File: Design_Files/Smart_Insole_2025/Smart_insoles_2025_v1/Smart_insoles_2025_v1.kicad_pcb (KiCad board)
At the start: 4 copper layers, 69.7 x 30.1 mm, 101 parts, among them IC1 USBLC6-2SC6, J1 Conn_01x20, J2 USB_C_Receptacle_USB2.0_16P, J4 S2B-PH-SM4-TB_LF__SN_, Q2 FDN306P, SW1 RESET, SW2 BOOT, SW3 SW_Nidec_CAS-120A1, U1 ME6211C33M5, U2 CD74HC4067M96, U3 LSM6DSO32TR, U5 ESP32-C3-MINI-1-N4, U7 BQ24040DSQR, U8 MCP6004-I_ST, U9 MCP6004-I_ST

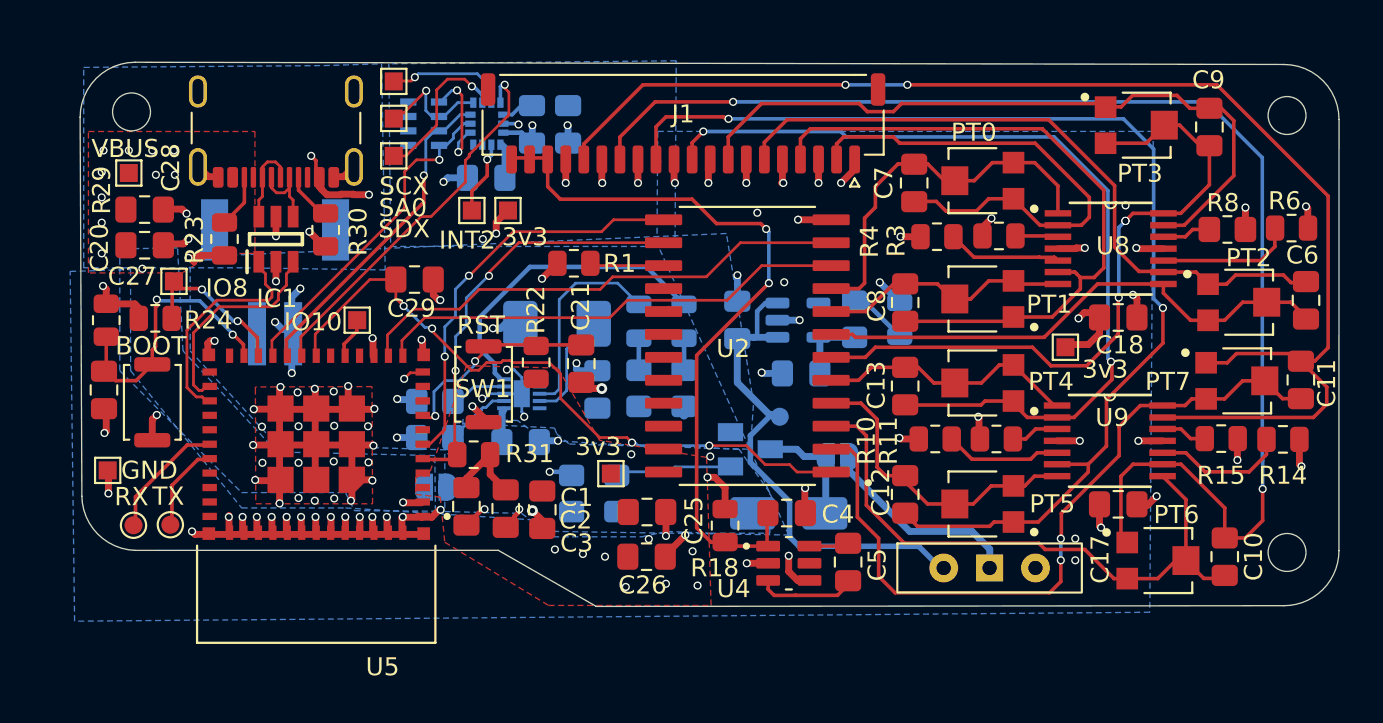
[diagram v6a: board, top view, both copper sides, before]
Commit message: PCB:Fixed Multiplexer wrong footprint. Flex Connector modified. Fixed DRC Errors and Warnings
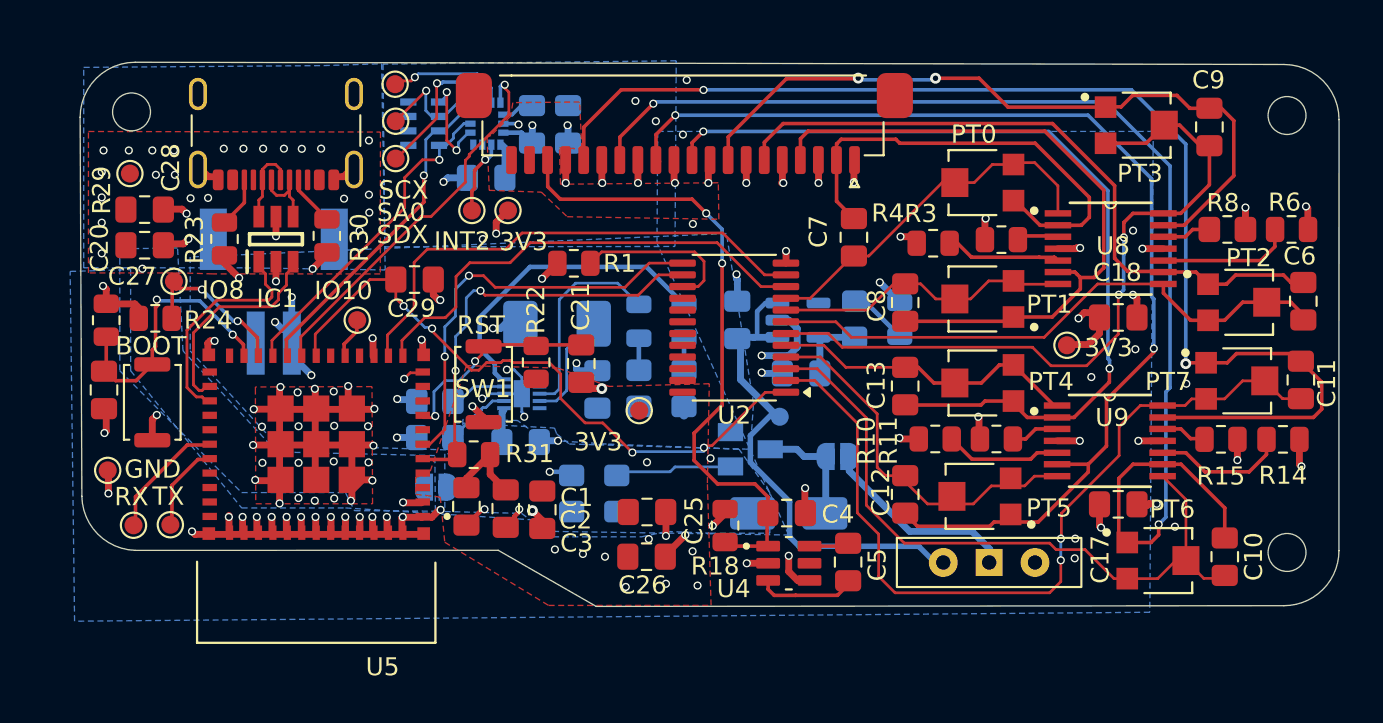
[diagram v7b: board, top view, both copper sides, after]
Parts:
- removed 3v3 (x3), GND, INT2, IO10, IO8, SA0, SCX, SDX, VBUS: TestPoint_Alt, TestPoint:TestPoint_Pad_1.0x1.0mm
- added TP1: TestPoint_Alt, TestPoint:TestPoint_Pad_D1.0mm, F.Cu at (106.3, 91.5)
- added TP10: TestPoint_Alt, TestPoint:TestPoint_Pad_D1.0mm, F.Cu at (122.2, 70.1)
- added TP11: TestPoint_Alt, TestPoint:TestPoint_Pad_D1.0mm, F.Cu at (126.5, 77.1)
- added TP12: TestPoint_Alt, TestPoint:TestPoint_Pad_D1.0mm, F.Cu at (135.8, 88.2)
- added TP13: TestPoint_Alt, TestPoint:TestPoint_Pad_D1.0mm, F.Cu at (159.5, 84.6)
- added TP14: TestPoint_Alt, TestPoint:TestPoint_Pad_D1.0mm, F.Cu at (122.3, 72.2)
- added TP2: TestPoint_Alt, TestPoint:TestPoint_Pad_D1.0mm, F.Cu at (128.5, 77.1)
- added TP3: TestPoint_Alt, TestPoint:TestPoint_Pad_D1.0mm, F.Cu at (107.6, 75.1)
- added TP7: TestPoint_Alt, TestPoint:TestPoint_Pad_D1.0mm, F.Cu at (110.0, 81.0)
- added TP8: TestPoint_Alt, TestPoint:TestPoint_Pad_D1.0mm, F.Cu at (120.2, 83.2)
- added TP9: TestPoint_Alt, TestPoint:TestPoint_Pad_D1.0mm, F.Cu at (122.3, 74.2)
- J2: footprint Connector_USB:USB_C_Receptacle_GCT_USB4105-xx-A_16P_TopMnt_Horizontal -> USB_C_Receptacle_16P_SMD_pins_THT_mech:USB_C_Receptacle_GCT_USB4105-xx-A_16P_TopMnt_Horizontal
- U2: footprint CD74HC4067:SOIC127P1030X265-24N -> Package_SO:TSSOP-24_4.4x7.8mm_P0.65mm
- moved C7 4.50 mm to (147.7, 78.6), turned to -90 degrees
- moved U2 1.24 mm to (141.0, 83.6)
- moved J4 0.52 mm to (115.5, 84.5)
- moved PT5 0.45 mm to (154.5, 93.0)
- moved R4 0.42 mm to (152.1, 78.9)
- moved R30 0.34 mm to (118.5, 78.5)
- moved SW3 0.31 mm to (155.2, 96.6)
- moved R3 0.25 mm to (155.8, 78.7)
- moved C6 0.16 mm to (172.6, 82.2)
- moved J2 0.14 mm to (115.7, 71.8)
- moved PT0 0.11 mm to (154.7, 75.6)
- moved R6 0.08 mm to (171.9, 78.2)
- renumbered VSEL to TP4
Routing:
- net /FSR_AnalogFE/FSR_OUT_7: track 74.1 -> 68.2 mm
- net Net-(U2-~{E}): track 3.96 -> 9.30 mm
- net I7: track 40.9 -> 46.1 mm
- net /FSR_AnalogFE/FSR_OUT_6: track 73.9 -> 69.1 mm
- net /FSR_AnalogFE/FSR_IN: track 41.3 -> 36.7 mm
- net VBUS: track 6.06 -> 1.49 mm, vias 14 -> 25
- net I6: track 33.7 -> 38.1 mm
- net I5: track 16.8 -> 21.1 mm
- net I2: track 29.6 -> 32.4 mm
- net I4: track 14.5 -> 17.2 mm
- net I3: track 38.0 -> 40.6 mm, vias 3 -> 2
- net I1: track 14.0 -> 16.5 mm
- net /FSR_AnalogFE/FSR_OUT_0: track 28.3 -> 26.5 mm
- net /FSR_AnalogFE/FSR_OUT_5: track 64.3 -> 62.7 mm
- net SIG: track 37.9 -> 36.4 mm
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- added copper zone on F.Cu, net /FSR_AnalogFE/FSR_IN
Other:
- board text added: "3V3"
- board text added: "GND"
- board text added: "INT2"
- board text added: "IO10"
- board text added: "IO8"
- board text added: "SA0"
- board text added: "SCX"
- board text added: "SDX"

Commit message: Modified some footprints to better fit real components.
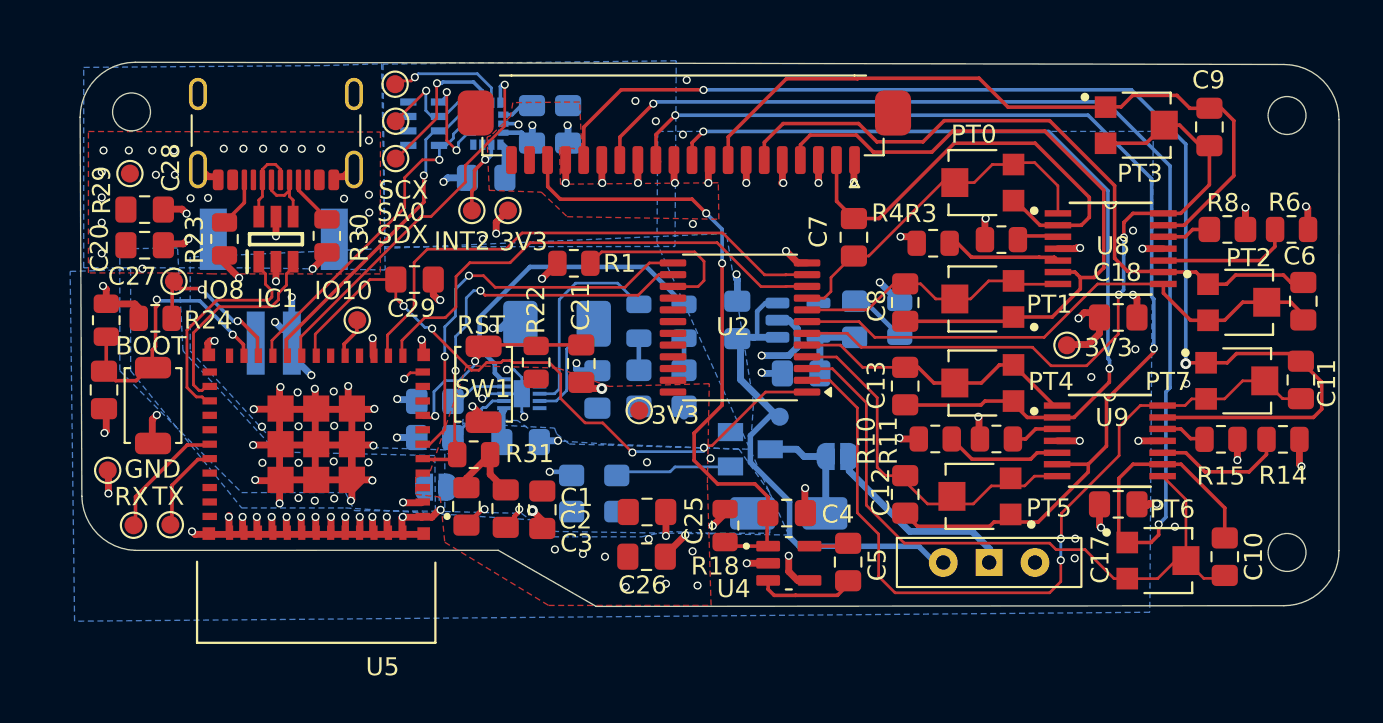
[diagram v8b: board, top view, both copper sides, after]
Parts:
- U2: footprint Package_SO:TSSOP-24_4.4x7.8mm_P0.65mm -> Package_SO:TSSOP-24_6.1x7.8mm_P0.65mm
- moved U2 0.32 mm to (141.4, 83.6)
- moved SW2 0.18 mm to (108.8, 87.9)
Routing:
- net GND: track 157.7 -> 166.5 mm
- net I5: track 21.1 -> 19.7 mm
- net I6: track 38.1 -> 36.8 mm
- net S1: track 28.1 -> 29.2 mm
- net S0: track 26.4 -> 27.6 mm
- net SIG: track 36.4 -> 37.6 mm
- net I3: track 40.6 -> 39.4 mm
- net I4: track 17.2 -> 16.1 mm
- net I2: track 32.4 -> 31.2 mm
- net I1: track 16.5 -> 15.3 mm
- net I7: track 46.1 -> 45.0 mm
- net /FSR_AnalogFE/FSR_OUT_2: track 37.6 -> 38.5 mm
- net I0: track 20.2 -> 19.5 mm
- net /FSR_AnalogFE/FSR_OUT_1: track 37.2 -> 37.8 mm
- net Net-(U2-~{E}): track 9.30 -> 9.83 mm
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- removed copper zone on F.Cu, net GND
